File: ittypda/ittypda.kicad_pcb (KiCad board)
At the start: 2 copper layers, 105 x 109.8 mm, 175 parts, among them CN1 S2B-PH-SM4-TB, J1 USB_C_Receptacle_USB2.0_14P, J13 Conn_01x05_Pin, J14 Conn_01x05_Pin, J2 Conn_01x04_Pin, SW1 Switch, SW10 Switch, SW11 Switch, SW12 Switch, SW13 Switch, SW14 Switch, SW15 Switch, SW16 Switch, SW17 Switch, SW18 Switch, SW19 Switch, SW2 Switch, SW20 Switch, SW21 Switch, SW22 Switch, SW23 Switch, SW24 Switch, SW25 SLIDE SWITCH, SW26 Switch, SW27 Switch, SW28 Switch, SW29 Switch, SW3 Switch, SW30 Switch, SW31 Switch, SW32 Switch, SW33 Switch, SW34 Switch, SW36 Switch, SW37 Switch, SW38 Switch, SW39 Switch, SW4 Switch, SW41 Switch, SW42 Switch, SW43 Switch, SW44 Switch, SW45 Switch, SW46 Switch, SW47 Switch, SW48 Switch, SW49 Switch, SW5 Switch, SW50 Switch, SW51 Switch, SW52 Switch, SW53 Switch, SW54 Switch, SW55 Switch, SW56 Switch, SW57 Switch, SW58 Switch, SW59 Switch, SW6 Switch, SW60 Switch, SW61 Switch, SW7 Switch, SW8 Switch, SW9 Switch, U1 TPS63001, U2 BQ24040DSQR, U4 STM32F411RETx, Y1 16Mhz

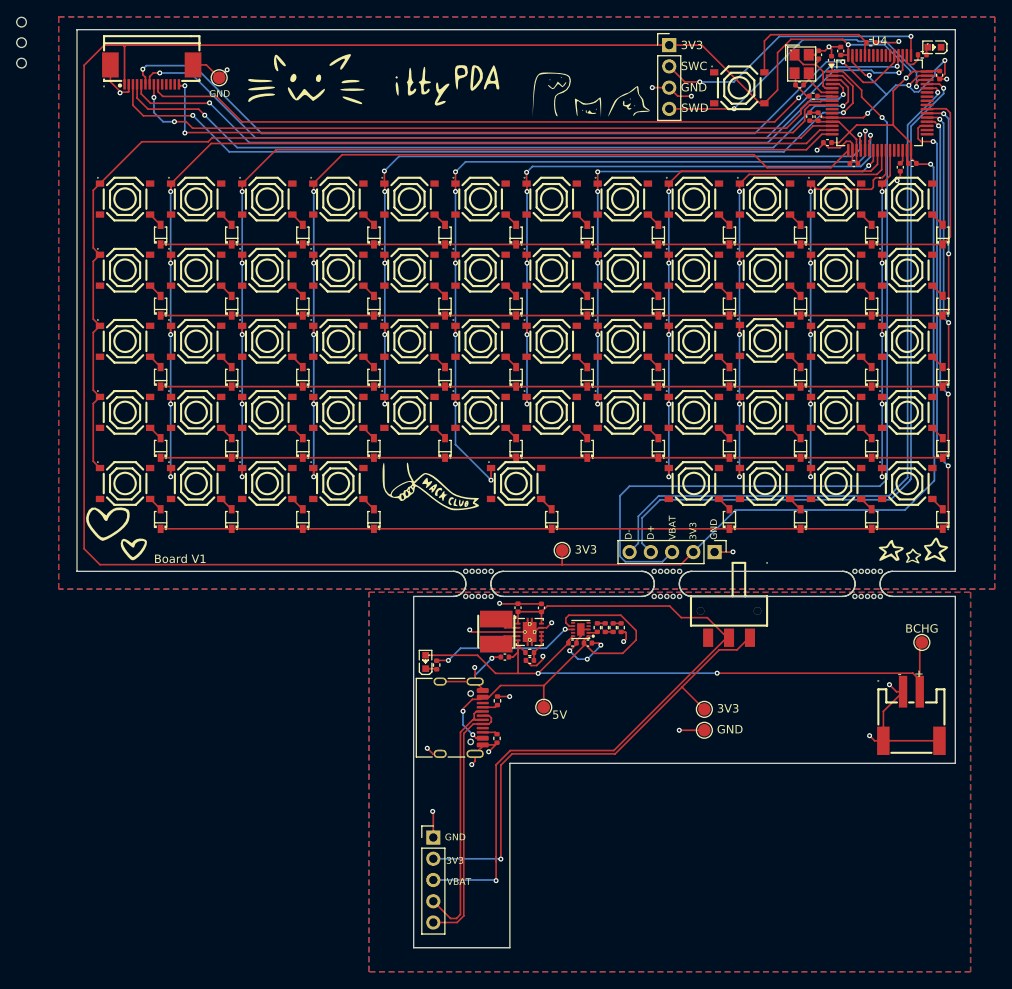
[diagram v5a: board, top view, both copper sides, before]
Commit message: add battery value reading to pcb !!
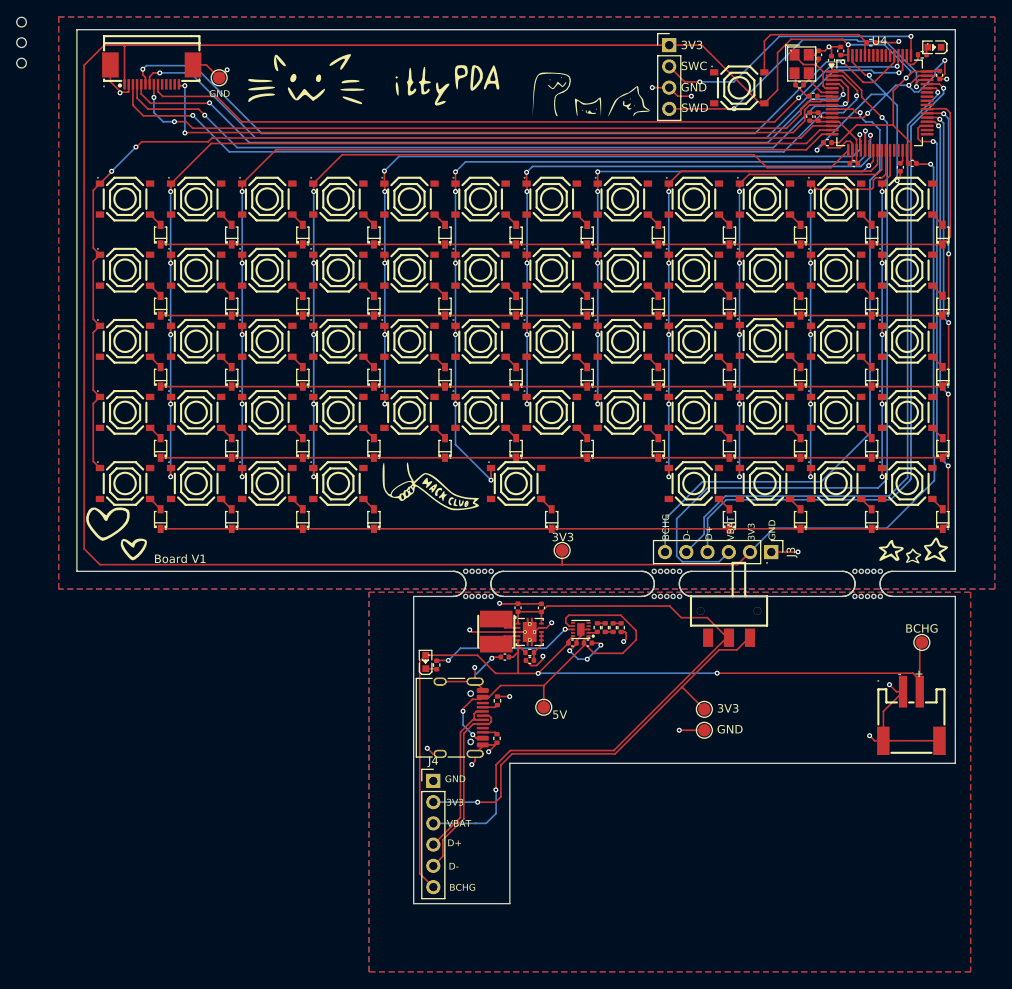
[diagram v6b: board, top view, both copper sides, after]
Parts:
- removed J13, J14: Conn_01x05_Pin, Connector_PinHeader_2.54mm:PinHeader_1x05_P2.54mm_Vertical
- added J3: Conn_01x06_Pin, Connector_PinHeader_2.54mm:PinHeader_1x06_P2.54mm_Vertical, F.Cu at (107.0, 93.2)
- added J4: Conn_01x06_Pin, Connector_PinHeader_2.54mm:PinHeader_1x06_P2.54mm_Vertical, F.Cu at (66.6, 120.5)
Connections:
- U4 pad 10: unconnected-(U4-PC2-Pad10) -> InBCHG
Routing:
- net InBCHG: track 0.00 -> 76.4 mm, vias 0 -> 1
- net BCHGOUT: track 82.8 -> 111.5 mm
- net GND: track 154.3 -> 174.1 mm, vias 32 -> 31
- net OutD+: track 31.3 -> 20.0 mm
- net OutD-: track 31.2 -> 22.8 mm
- net InVBAT: track 100.1 -> 91.7 mm
- net InD+: track 89.1 -> 80.8 mm
- net OutVBAT: track 85.2 -> 77.6 mm
- net InD-: track 88.0 -> 80.5 mm
- net Out3V3: track 59.0 -> 51.8 mm
- net Col0: track 127.0 -> 127.1 mm, vias 0 -> 2
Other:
- board size 105 x 109.8 mm -> 105 x 104.5 mm

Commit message: add voltage divider to battery reading
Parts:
- removed H1, H2, H3: MountingHole, MountingHole:ToolingHole_1.152mm
- added R13: 100k, Resistor_SMD:R_0402_1005Metric, F.Cu at (73.1, 126.7)
- added R14: 200k, Resistor_SMD:R_0402_1005Metric, F.Cu at (73.1, 127.7)
- added R15: 100k, Resistor_SMD:R_0402_1005Metric, F.Cu at (73.1, 128.6)
- added R16: 51k, Resistor_SMD:R_0402_1005Metric, F.Cu at (73.1, 129.6)
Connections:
- J4 pad 6: BCHGOUT -> BCHGOUT_Divided
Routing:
- net BCHGOUT_Divided: track 0.00 -> 13.8 mm
- net BCHGOUT: track 111.5 -> 119.3 mm
- net GND: track 174.1 -> 177.8 mm, vias 31 -> 33
- net Net-(R15-Pad2): track 0.00 -> 0.95 mm
- net Net-(R14-Pad2): track 0.00 -> 0.95 mm
